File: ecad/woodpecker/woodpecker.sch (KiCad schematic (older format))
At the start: 0 parts

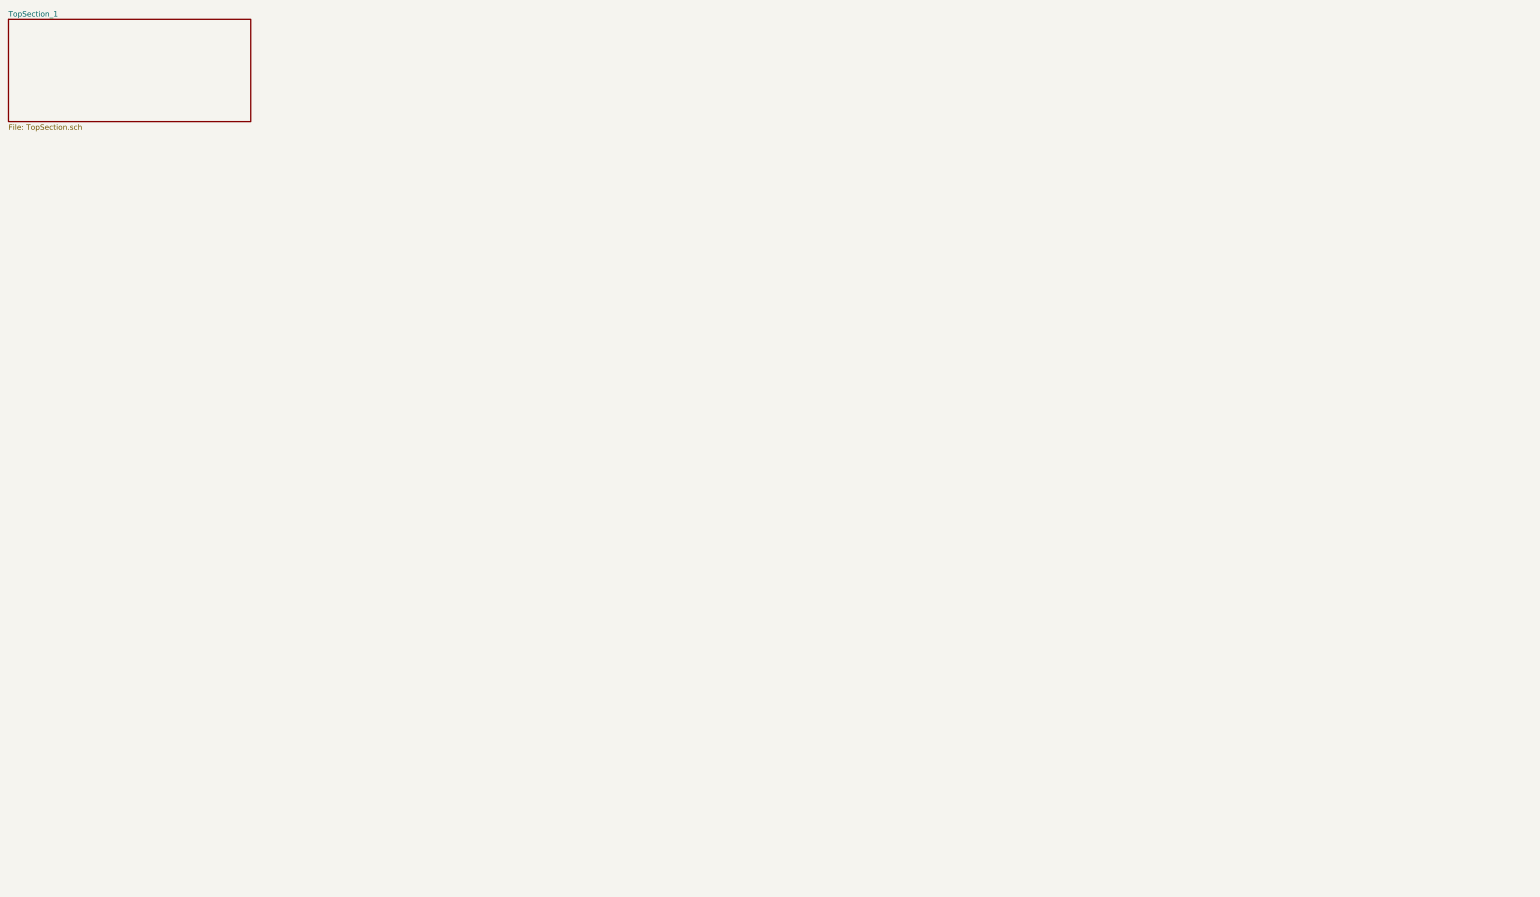
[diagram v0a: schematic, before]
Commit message: Adds bottom section in monolithic design
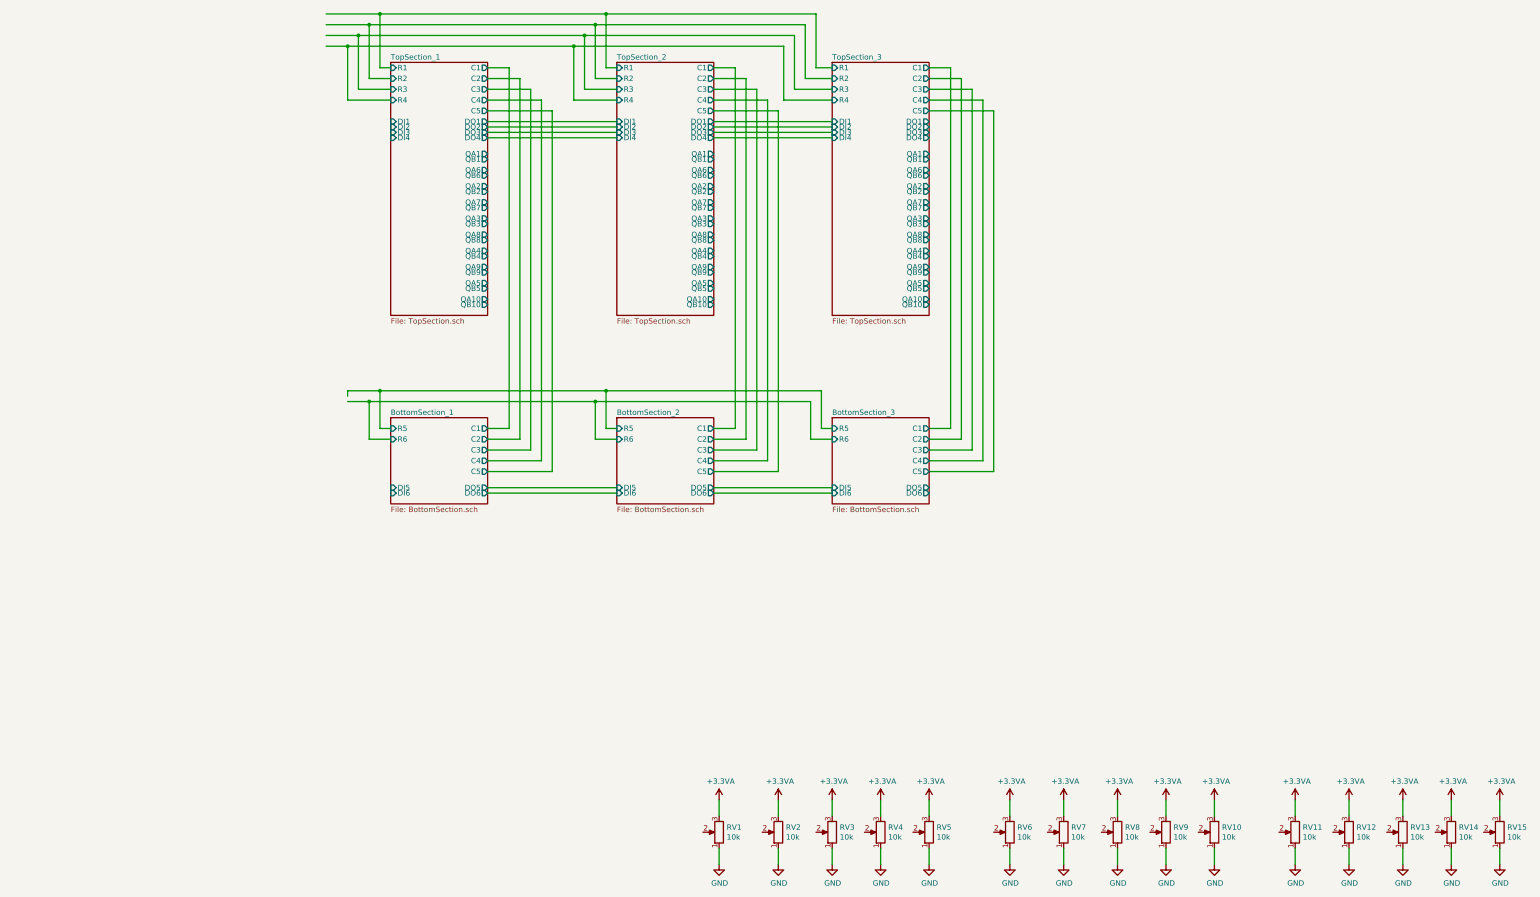
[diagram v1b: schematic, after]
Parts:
- added RV1, RV10, RV11, RV12, RV13, RV14, RV15, RV2, RV3, RV4, RV5, RV6, RV7, RV8, RV9: 10k, woodpecker:Potentiometer_Bourns_PTA6043_Single_Slide, symbol Device:R_POT
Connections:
- net labels added: +3.3VA, GND
- wire segments 0 -> 142
